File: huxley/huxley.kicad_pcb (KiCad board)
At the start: 4 copper layers, 150 x 150 mm, 102 parts, among them J1 CT3151V1-2, J11 SMA_RF2-04A-T-00-50-G, J13 SMA_RF2-04A-T-00-50-G, J15 SMA_RF2-04A-T-00-50-G, J17 SMA_RF2-04A-T-00-50-G, J18 SMA_RF2-04A-T-00-50-G, J19 SMA_RF2-04A-T-00-50-G, J2 CT3151V1-2, J20 SMA_RF2-04A-T-00-50-G, J21 61300211121, J22 SMA_RF2-04A-T-00-50-G, J24 CT3151V1-2, J25 61300211121, J26 61300211121, J27 61300211121, J28 61300211121, J29 61300211121, J3 CT3151V1-2, J30 61300211121, J31 61300211121, J32 61300211121, J34 CT3151V1-0, J35 CT3151V1-2, J37 CT3151V1-0, J39 CT3151V1-2, J4 SMA_RF2-04A-T-00-50-G, J5 SMA_RF2-04A-T-00-50-G, J7 SMA_RF2-04A-T-00-50-G, J9 SMA_RF2-04A-T-00-50-G, U2 LM134H, U3 MAX40201FAUA+, U4 TMUX1112PWR, U5 TMUX1112PWR, U6 NVT2010PW_118

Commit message: layout_1010
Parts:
- added C44: 1n, Capacitor_SMD:C_0603_1608Metric, F.Cu at (83.8, 152.9)
- added C45: 10p, Capacitor_SMD:C_0603_1608Metric, F.Cu at (81.2, 152.9)
- added C46: 1n, Capacitor_SMD:C_0603_1608Metric, F.Cu at (78.7, 152.9)
- added C47: 10p, Capacitor_SMD:C_0603_1608Metric, F.Cu at (76.2, 152.9)
- added C48: 1n, Capacitor_SMD:C_0603_1608Metric, F.Cu at (127.2, 144.3)
- added C49: 1n, Capacitor_SMD:C_0603_1608Metric, F.Cu at (124.7, 144.3)
- added C50: 10p, Capacitor_SMD:C_0603_1608Metric, F.Cu at (132.0, 144.4)
- added C51: 10p, Capacitor_SMD:C_0603_1608Metric, F.Cu at (129.5, 144.4)
- added C52: 1n, Capacitor_SMD:C_0603_1608Metric, F.Cu at (74.8, 75.5)
- added C53: 1n, Capacitor_SMD:C_0603_1608Metric, F.Cu at (72.3, 75.5)
- added C54: 10p, Capacitor_SMD:C_0603_1608Metric, F.Cu at (69.8, 75.5)
- added C55: 10p, Capacitor_SMD:C_0603_1608Metric, F.Cu at (67.3, 75.5)
- added C56: 1n, Capacitor_SMD:C_0603_1608Metric, F.Cu at (68.6, 35.6)
- added C57: 1n, Capacitor_SMD:C_0603_1608Metric, F.Cu at (68.6, 38.1)
- added C58: 10p, Capacitor_SMD:C_0603_1608Metric, F.Cu at (68.6, 40.6)
- added C59: 10p, Capacitor_SMD:C_0603_1608Metric, F.Cu at (68.6, 43.1)
- added C60: 1n, Capacitor_SMD:C_0603_1608Metric, F.Cu at (93.5, 79.6)
- added C61: 1n, Capacitor_SMD:C_0603_1608Metric, F.Cu at (93.5, 82.1)
- added C62: 10p, Capacitor_SMD:C_0603_1608Metric, F.Cu at (93.5, 84.6)
- added C63: 10p, Capacitor_SMD:C_0603_1608Metric, F.Cu at (93.5, 87.1)
- added C64: x, Capacitor_SMD:C_0603_1608Metric, F.Cu at (143.5, 123.7)
- added C65: x, Capacitor_SMD:C_0603_1608Metric, F.Cu at (143.5, 129.0)
- added C66: x, Capacitor_SMD:C_0603_1608Metric, F.Cu at (143.8, 116.3)
- added C67: x, Capacitor_SMD:C_0603_1608Metric, F.Cu at (143.8, 109.7)
- added C68: x, Capacitor_SMD:C_0603_1608Metric, F.Cu at (143.5, 102.6)
- added C69: x, Capacitor_SMD:C_0603_1608Metric, F.Cu at (143.5, 96.3)
- added C70: x, Capacitor_SMD:C_0603_1608Metric, F.Cu at (71.1, 99.3)
- added C71: x, Capacitor_SMD:C_0603_1608Metric, F.Cu at (71.4, 105.4)
- added C72: x, Capacitor_SMD:C_0603_1608Metric, F.Cu at (71.4, 117.1)
- added C73: x, Capacitor_SMD:C_0603_1608Metric, F.Cu at (71.1, 111.5)
- added C74: x, Capacitor_SMD:C_0603_1608Metric, F.Cu at (71.6, 123.2)
- added C75: x, Capacitor_SMD:C_0603_1608Metric, F.Cu at (71.4, 129.0)
- C1, C10, C11, C12, C2, C3, C4, C5, C6, C7, C8, C9: footprint Capacitor_SMD:C_0402_1005Metric -> Capacitor_SMD:C_0603_1608Metric
- C17, C18: value 10u -> 0.1u
- C21, C25, C29, C33, C41: value 0.1u -> 1u
- C22, C26, C30, C34, C42: value 1n -> 0.1u
- C23, C27, C31, C35, C43: value 10p -> 0.1u
- U2: footprint 0_726_footprints:lm134 -> Package_TO_SOT_THT:TO-46-3
- turned U2 to 0 degrees

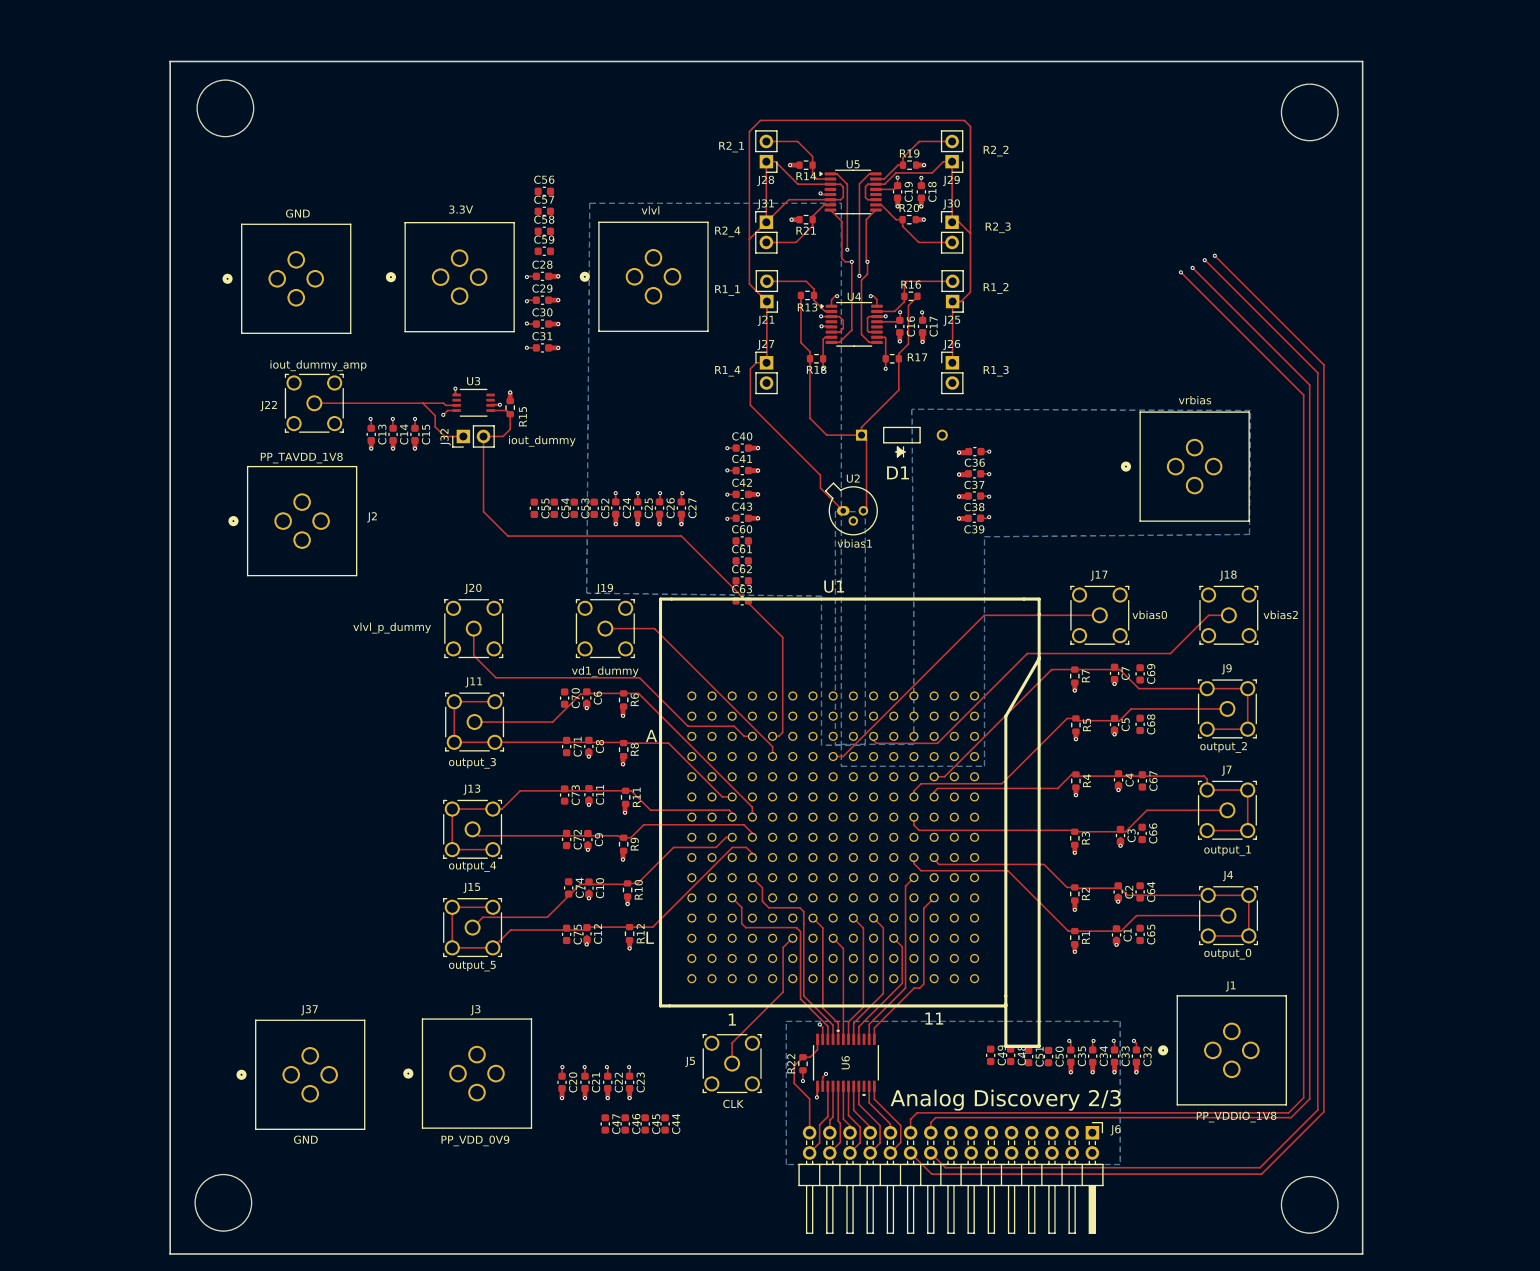
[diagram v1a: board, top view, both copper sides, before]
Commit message: minor schematic cleanup; addition of mounting holes; minor layout adjustment
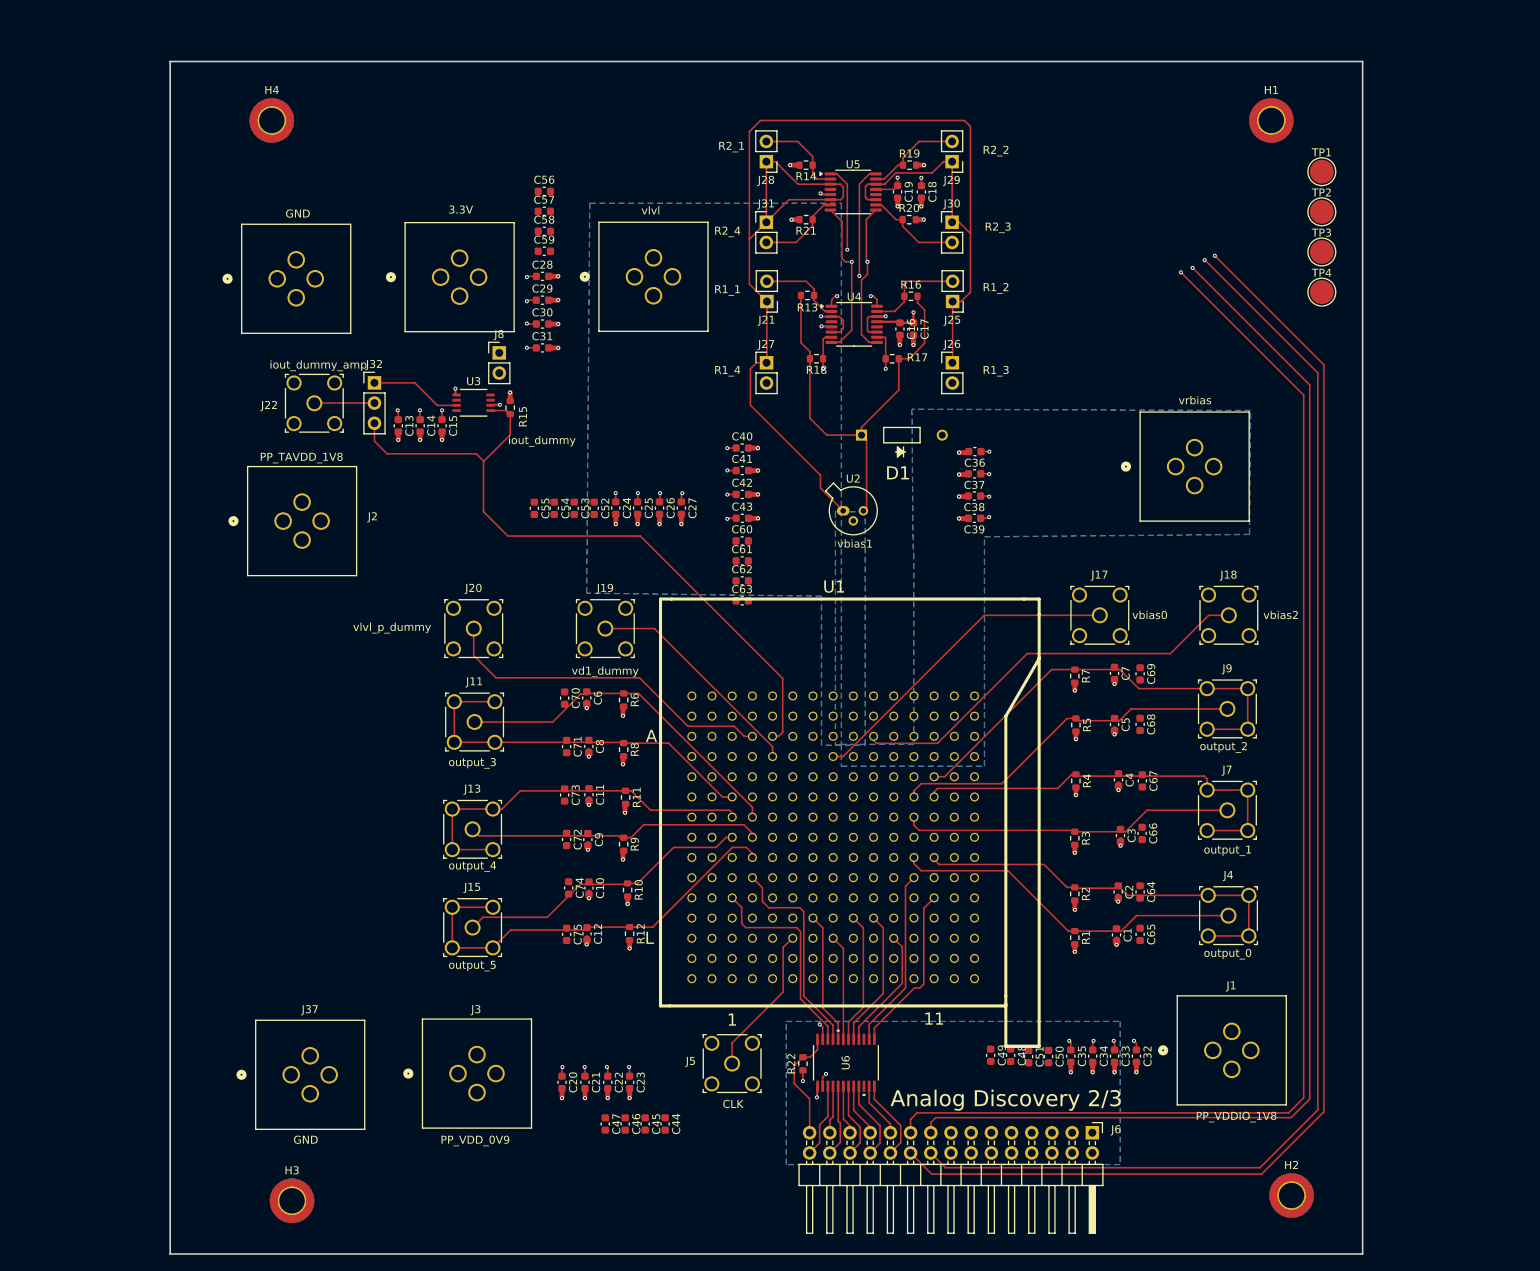
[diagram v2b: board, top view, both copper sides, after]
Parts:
- added H1: MountingHole, MountingHole:MountingHole_3.2mm_M3_DIN965_Pad_TopBottom, F.Cu at (160.0, 26.7)
- added H2: MountingHole, MountingHole:MountingHole_3.2mm_M3_DIN965_Pad_TopBottom, F.Cu at (162.6, 161.9)
- added H3: MountingHole, MountingHole:MountingHole_3.2mm_M3_DIN965_Pad_TopBottom, F.Cu at (36.8, 162.6)
- added H4: MountingHole, MountingHole:MountingHole_3.2mm_M3_DIN965_Pad_TopBottom, F.Cu at (34.3, 26.7)
- added J8: 61300211121, Connector_PinHeader_2.54mm:PinHeader_1x02_P2.54mm_Vertical, F.Cu at (62.9, 55.9)
- added TP1: TestPoint, TestPoint:TestPoint_Pad_D3.0mm, F.Cu at (166.4, 33.1)
- added TP2: TestPoint, TestPoint:TestPoint_Pad_D3.0mm, F.Cu at (166.4, 38.2)
- added TP3: TestPoint, TestPoint:TestPoint_Pad_D3.0mm, F.Cu at (166.4, 43.2)
- added TP4: TestPoint, TestPoint:TestPoint_Pad_D3.0mm, F.Cu at (166.4, 48.3)
- J32: footprint Connector_PinHeader_2.54mm:PinHeader_1x02_P2.54mm_Vertical -> Connector_PinHeader_2.54mm:PinHeader_1x03_P2.54mm_Vertical
- moved J32 13.1 mm to (47.2, 59.7), turned to 0 degrees
- moved C13 3.58 mm to (50.2, 65.1)
- moved C14 3.58 mm to (53.0, 65.1)
- moved C15 3.58 mm to (55.7, 65.1)
- moved C17 1.19 mm to (115.0, 52.9)
- moved C16 0.32 mm to (113.3, 52.9)
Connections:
- J22 pad 1: iout_dummy_amp -> iout_dummy_amp_conn
- J32 pad 2: iout_dummy -> iout_dummy_amp_conn
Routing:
- net iout_dummy_amp: track 25.7 -> 11.5 mm
- net iout_dummy: track 75.4 -> 87.9 mm
- net iout_dummy_amp_conn: track 0.00 -> 7.57 mm
- net Net-(D1-A): track 53.6 -> 55.1 mm
- net PP_SYS_3V3: track 20.2 -> 19.5 mm, vias 12 -> 10
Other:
- outline, holes or cut-outs redrawn

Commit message: changed output names to be kicad diffpair-style (+/-); board rearrangement wip
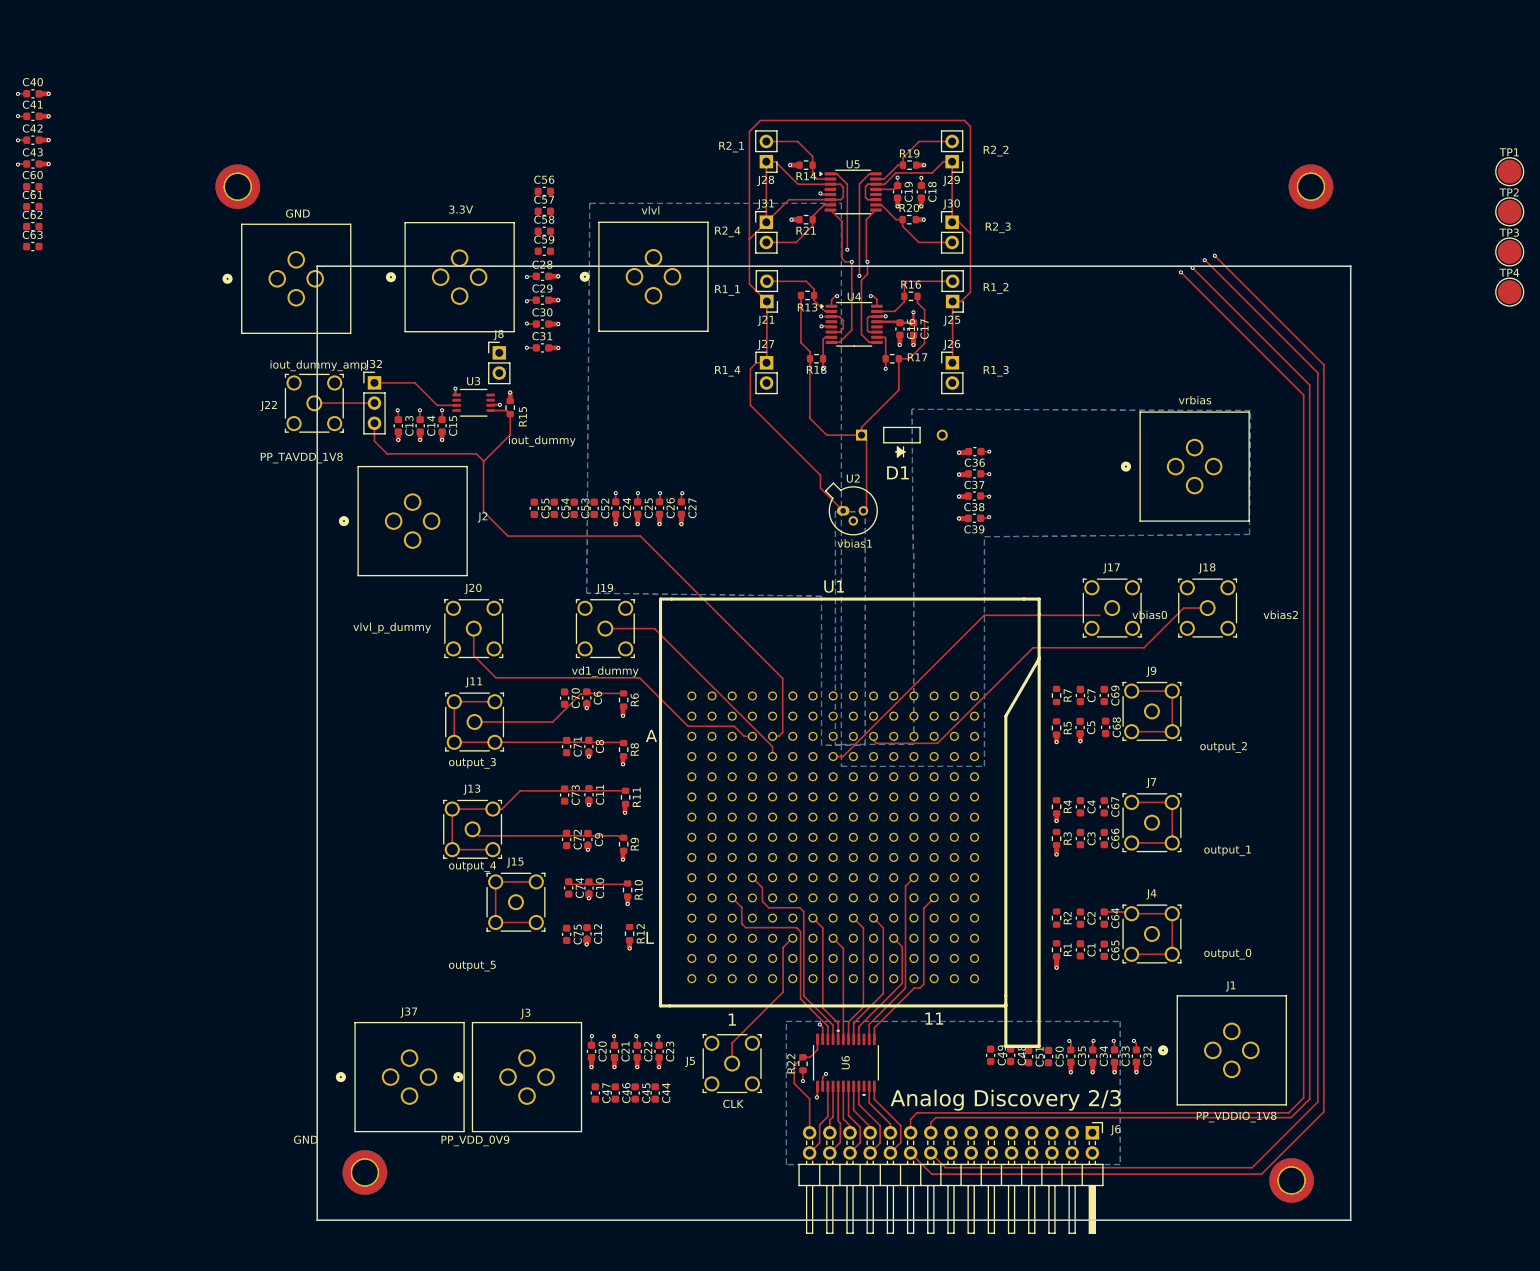
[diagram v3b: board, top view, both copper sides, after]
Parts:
- moved C60 99.7 mm to (4.22, 35.0)
- moved C61 99.7 mm to (4.22, 37.5)
- moved C62 99.7 mm to (4.22, 40.0)
- moved C63 99.7 mm to (4.22, 42.5)
- moved C40 99.7 mm to (4.24, 23.3)
- moved C41 99.7 mm to (4.24, 26.1)
- moved C42 99.7 mm to (4.24, 29.1)
- moved C43 99.7 mm to (4.24, 32.1)
- moved TP1 23.6 mm to (190.0, 33.1)
- moved TP2 23.6 mm to (190.0, 38.2)
- moved TP3 23.6 mm to (190.0, 43.2)
- moved TP4 23.6 mm to (190.0, 48.3)
- moved J2 13.9 mm to (49.6, 77.1)
- moved J37 12.5 mm to (49.2, 147.0)
- moved J4 9.90 mm to (145.0, 129.0)
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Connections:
- net output_0a renamed output_0+
- net output_0b renamed output_0-
- net output_1a renamed output_1+
- net output_1b renamed output_1-
- net output_2a renamed output_2+
- net output_2b renamed output_2-
- net output_3a renamed output_3+
- net output_3b renamed output_3-
- net output_4a renamed output_4+
- net output_4b renamed output_4-
- net output_5a renamed output_5+
- net output_5b renamed output_5-
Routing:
- net output_2+: track 44.7 -> 0.00 mm
- net output_0+: track 44.7 -> 0.00 mm
- net output_3+: track 43.6 -> 0.00 mm
- net output_1+: track 41.9 -> 0.89 mm
- net output_2-: track 56.2 -> 15.3 mm
- net output_5-: track 54.0 -> 15.3 mm
- net output_1-: track 52.8 -> 15.4 mm
- net output_0-: track 51.9 -> 18.9 mm
- net output_5+: track 37.4 -> 7.78 mm
- net (no net): track 0.00 -> 20.2 mm
- net output_4+: track 37.3 -> 19.4 mm
- net output_3-: track 48.0 -> 31.6 mm
- net output_4-: track 48.0 -> 33.0 mm
- net GND: track 69.7 -> 64.7 mm, vias 65 -> 58
- net vbias2: track 52.0 -> 49.7 mm
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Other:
- board size 150 x 150 mm -> 130 x 120 mm

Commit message: temp mid-rearrange
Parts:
- moved D1 14.2 mm to (110.4, 80.3)
- moved R20 12.8 mm to (114.4, 51.9)
- moved R21 12.8 mm to (101.4, 51.9)
- moved J28 12.8 mm to (96.4, 44.6)
- moved J29 12.8 mm to (119.8, 44.6)
- moved C16 12.8 mm to (113.2, 65.7)
- moved C17 12.8 mm to (114.9, 65.7)
- moved C18 12.8 mm to (115.9, 48.4)
- moved C19 12.8 mm to (112.9, 48.4)
- moved J21 12.8 mm to (96.5, 62.2)
- moved J25 12.8 mm to (119.8, 62.2)
- moved J26 12.8 mm to (119.8, 69.9)
- moved J27 12.8 mm to (96.4, 69.9)
- moved J30 12.8 mm to (119.8, 52.2)
- moved J31 12.8 mm to (96.4, 52.2)
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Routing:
- net /ibias/ibias_rset: track 205.6 -> 124.9 mm
- net IBIAS_SEL4: track 224.1 -> 160.8 mm, vias 2 -> 1
- net IBIAS_SEL3: track 226.1 -> 164.7 mm, vias 2 -> 1
- net IBIAS_SEL1: track 235.8 -> 178.4 mm, vias 3 -> 2
- net IBIAS_SEL2: track 223.4 -> 168.1 mm, vias 3 -> 2
- net Net-(D1-A): track 55.1 -> 18.8 mm
- net (no net): track 20.2 -> 0.00 mm
- net output_4+: track 19.4 -> 0.00 mm
- net output_4-: track 33.0 -> 15.3 mm
- net output_3-: track 31.6 -> 15.3 mm
- net /ibias/R1_3: track 14.6 -> 5.02 mm
- net /ibias/R1_2: track 12.4 -> 22.0 mm
- net /ibias/R1_4: track 13.2 -> 4.88 mm
- net /ibias/R1_1: track 10.5 -> 18.8 mm
- net output_5+: track 7.78 -> 0.00 mm
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
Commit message: general rerrange struct inpl
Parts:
- moved J34 110.3 mm to (145.0, 54.0)
- moved C24 61.5 mm to (16.4, 68.8)
- moved C25 61.5 mm to (19.2, 68.8)
- moved C26 61.5 mm to (21.9, 68.8)
- moved C27 61.5 mm to (24.7, 68.8)
- moved C52 61.5 mm to (13.7, 68.9)
- moved C55 61.5 mm to (6.18, 68.9)
- moved C53 61.5 mm to (11.2, 68.9)
- moved C54 61.5 mm to (8.69, 68.9)
- moved J32 37.8 mm to (83.8, 69.5)
- moved R21 35.1 mm to (130.8, 71.1), turned to 0 degrees
- moved R15 35.1 mm to (95.4, 79.0)
- moved U3 35.1 mm to (90.8, 78.4)
- moved J35 34.8 mm to (89.6, 53.4)
- moved J31 33.8 mm to (124.5, 71.1), turned to 90 degrees
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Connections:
- net Net-(D1-A) renamed /ibias/ibias_m
- U4 pad 15: /ibias/R1_2 -> /ibias/R1_4
- U4 pad 16: IBIAS_SEL2 -> IBIAS_SEL4
- U4 pad 7: /ibias/R1_4 -> /ibias/R1_2
- U4 pad 8: IBIAS_SEL4 -> IBIAS_SEL2
- U5 pad 15: /ibias/R2_2 -> /ibias/R2_4
- U5 pad 16: IBIAS_SEL2 -> IBIAS_SEL4
- U5 pad 7: /ibias/R2_4 -> /ibias/R2_2
- U5 pad 8: IBIAS_SEL4 -> IBIAS_SEL2
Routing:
- net IBIAS_SEL1: track 178.4 -> 0.00 mm, vias 2 -> 0
- net IBIAS_SEL2: track 168.1 -> 0.00 mm, vias 2 -> 0
- net IBIAS_SEL3: track 164.7 -> 0.00 mm, vias 1 -> 0
- net IBIAS_SEL4: track 160.8 -> 0.00 mm, vias 1 -> 0
- net /ibias/ibias_rset: track 124.9 -> 21.2 mm, vias 2 -> 0
- net iout_dummy: track 86.4 -> 16.8 mm
- net output_3+: track 0.00 -> 39.5 mm
- net output_5-: track 15.3 -> 54.3 mm
- net output_2+: track 0.00 -> 36.5 mm
- net output_5+: track 0.00 -> 35.8 mm
- net output_0+: track 0.00 -> 34.5 mm
- net output_2-: track 15.3 -> 49.5 mm
- net output_3-: track 15.3 -> 49.1 mm
- net output_1+: track 0.89 -> 33.0 mm
- net output_4+: track 0.00 -> 31.8 mm
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- added copper zone on B.Cu, net /ibias/ibias_m
- added copper zone on F.Cu, net /ibias/ibias_rset
- removed copper zone on In2.Cu, net PP_SYS_3V3
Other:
- board size 130 x 120 mm -> 125 x 124 mm
